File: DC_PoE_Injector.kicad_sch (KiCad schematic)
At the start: 3 parts, among them U1 TPS23861

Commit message: Adding some skeleton
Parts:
- U1: LCSC (none) -> C93245
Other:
- added sheet Connectors (1_Connectors.kicad_sch)
- added sheet Power (2_Power.kicad_sch)

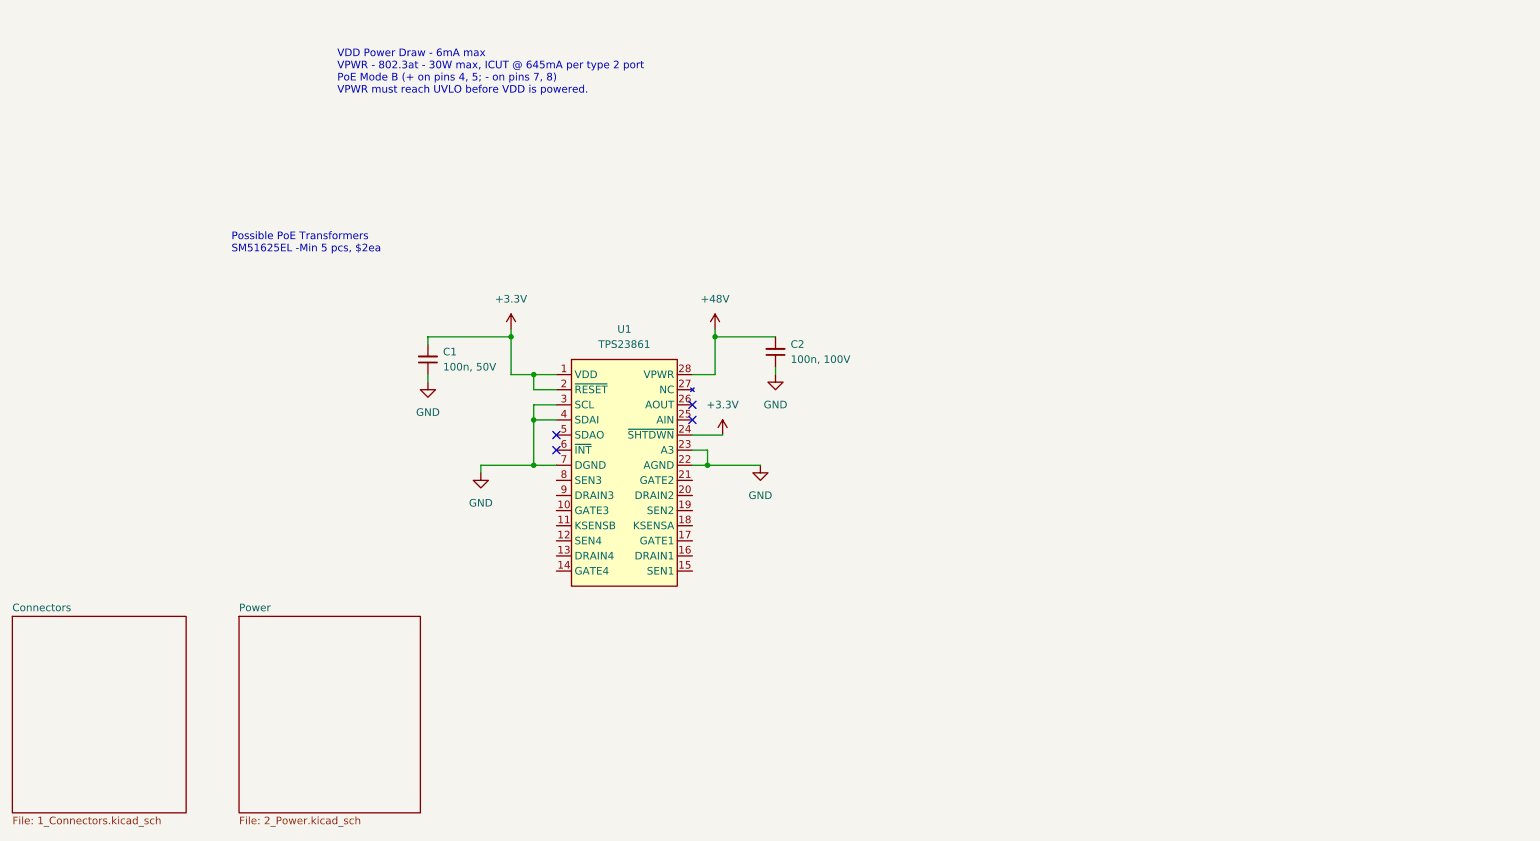
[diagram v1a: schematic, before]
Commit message: Add magnetics for poe
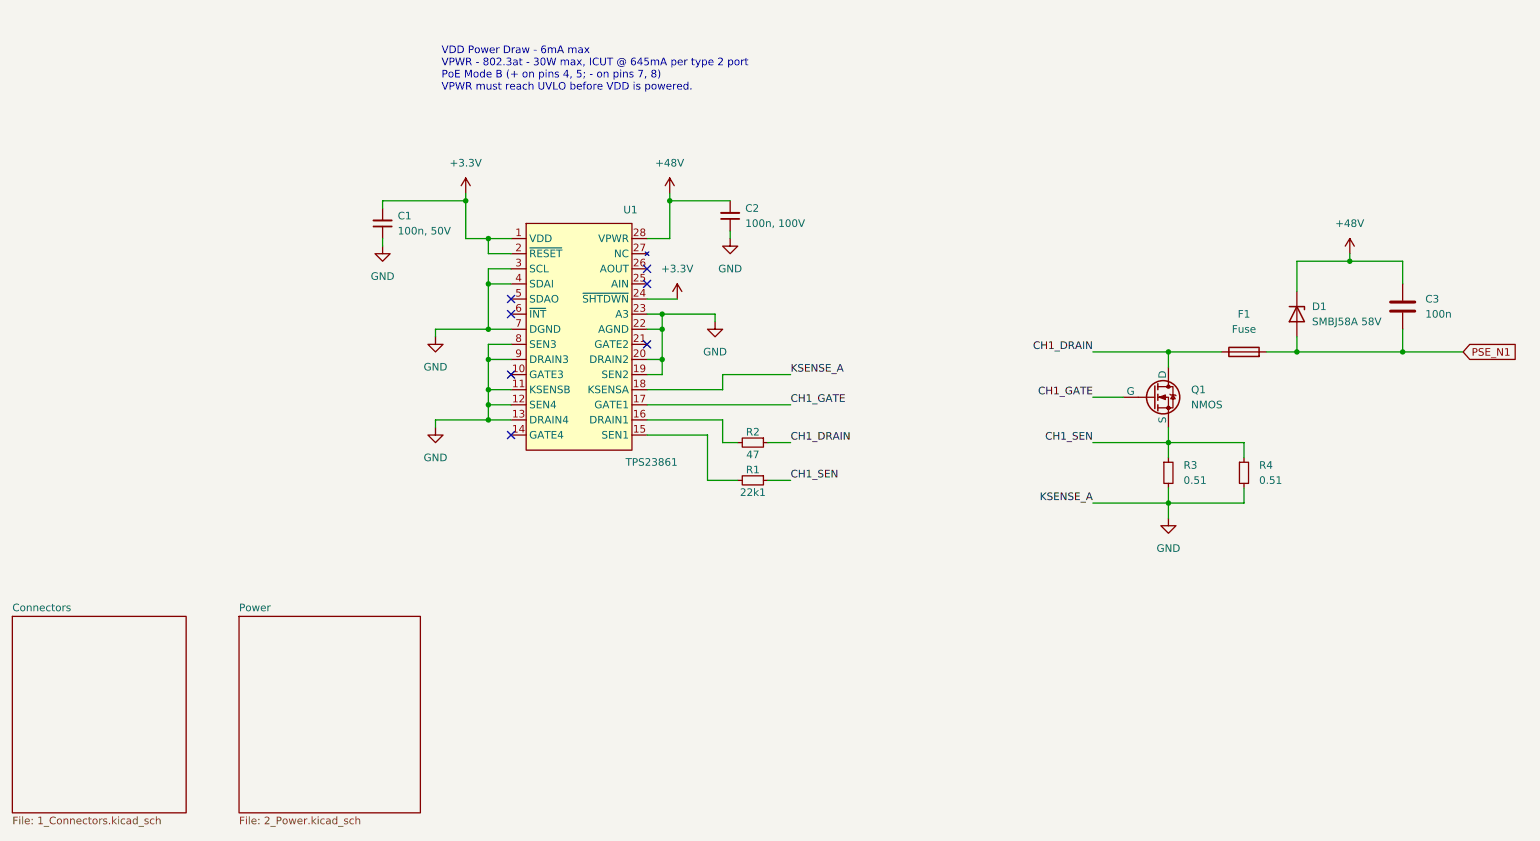
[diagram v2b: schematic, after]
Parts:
- added C3: 100n, symbol Device:C
- added D1: SMBJ58A 58V, symbol Device:D_Zener
- added F1: Fuse, symbol Device:Fuse
- added Q1: NMOS, symbol Simulation_SPICE:NMOS
- added R1: 22k1, symbol Device:R_Small
- added R2: 47, symbol Device:R_Small
- added R3, R4: 0.51, symbol Device:R_Small
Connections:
- net +48V: now also C3.1, D1.1 (K)
- net GND: now also U1.11 (KSENSB), U1.12 (SEN4), U1.13 (DRAIN4), U1.18 (KSENSA), U1.19 (SEN2), U1.20 (DRAIN2), U1.8 (SEN3), U1.9 (DRAIN3), R3.2, R4.2
- net at U1.15 (SEN1): now also R1.2
- net at U1.16 (DRAIN1): now also R2.2
- net CH1_GATE: now reaches U1.17 (GATE1)
- net CH1_GATE: now also Q1.2 (G)
- new net CH1_DRAIN: F1.1, Q1.1 (D), R2.1
- new net CH1_SEN: Q1.3 (S), R1.1, R3.1, R4.1
- new net PSE_N1: C3.2, D1.2 (A), F1.2
- no-connect marks 4 -> 7
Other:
- note removed: "Possible PoE Transformers SM51625EL -Min 5 pcs, $2ea"
- moved on the sheet: C1, C2, U1

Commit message: Add boost converter
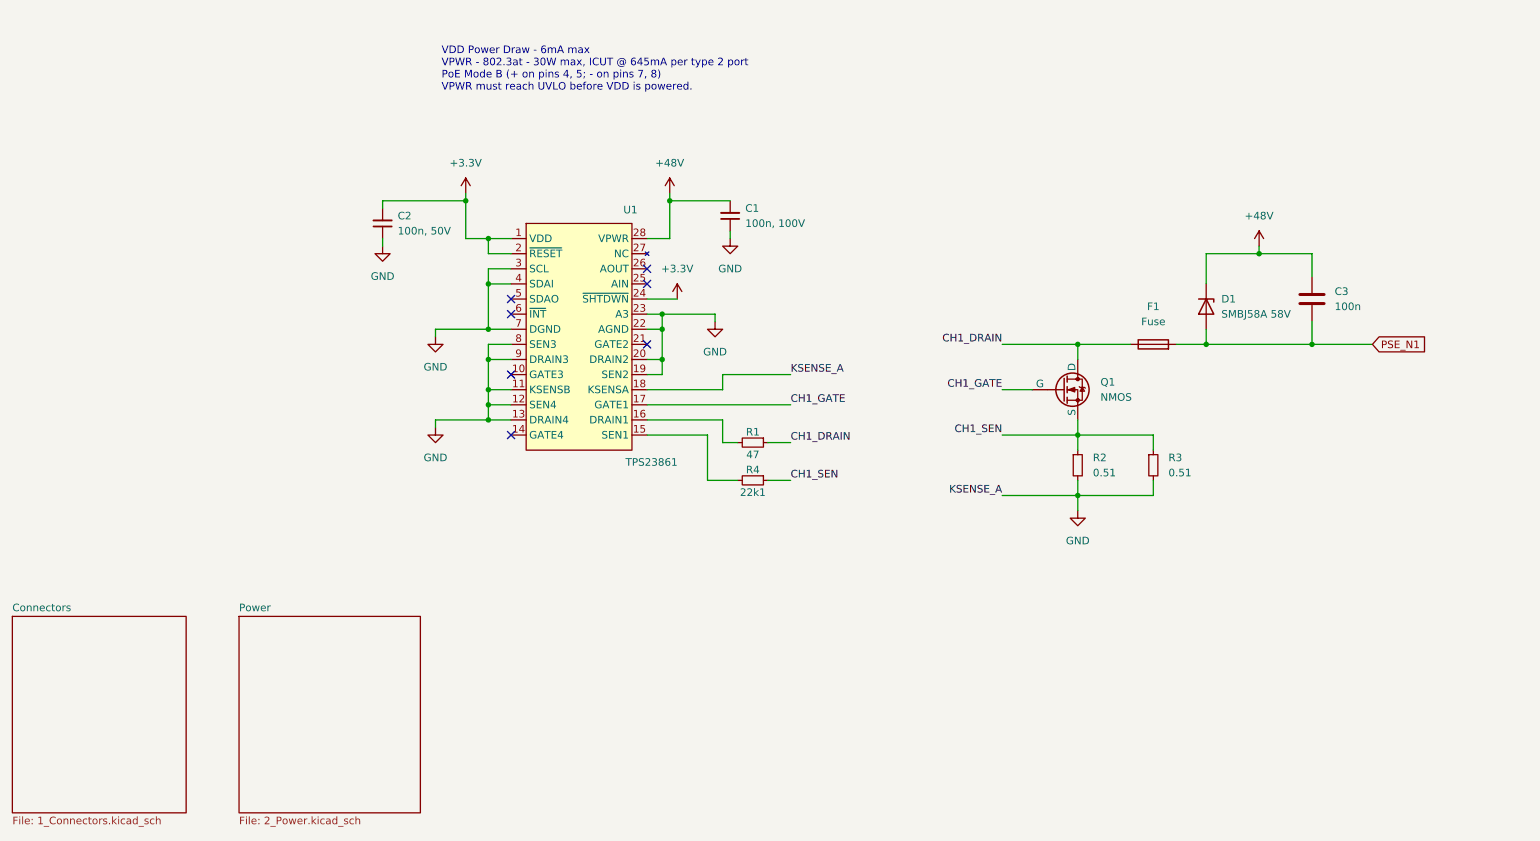
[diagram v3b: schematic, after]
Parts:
- renumbered C2 to C1, C1 to C2, R2 to R1, R3 to R2, R4 to R3, R1 to R4
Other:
- moved on the sheet: C3, D1, F1, Q1, R2, R3

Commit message: finish layout
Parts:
- removed C3: 100n, symbol Device:C
- removed Q1: NMOS, symbol Simulation_SPICE:NMOS
- added C3: 100n, 100V, Capacitor_SMD:C_0805_2012Metric, symbol Device:C_Small
- added C30: 1u, Capacitor_SMD:C_0805_2012Metric, symbol Device:C_Small
- added Q1: IRLR3410TRPBF, Package_TO_SOT_SMD:TO-252-2, symbol Device:Q_NMOS_GDS
- C1: footprint (none) -> Capacitor_SMD:C_0805_2012Metric; LCSC (none) -> C28233
- C2: footprint (none) -> Capacitor_SMD:C_0603_1608Metric; LCSC (none) -> C14663
- D1: footprint (none) -> Diode_SMD:D_SMB; LCSC (none) -> C135085
- F1: value Fuse -> 2920L110/60MR; footprint (none) -> Fuse:Fuse_2920_7451Metric; LCSC (none) -> C315903
- R1: footprint (none) -> Resistor_SMD:R_0603_1608Metric; LCSC (none) -> C23182
- R2, R3: value 0.51 -> 510m 1%; footprint (none) -> Resistor_SMD:R_0805_2012Metric; LCSC (none) -> C491234
- R4: value 22k1 -> 22.1; footprint (none) -> Resistor_SMD:R_0603_1608Metric; LCSC (none) -> C22958
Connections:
- net +3.3V: no longer U1.2 (~{RESET})
- net CH1_DRAIN: now also Q1.2 (D)
- net CH1_GATE: now also Q1.1 (G)
- net CH1_SEN: now also Q1.3 (S)
- net GND: now also C30.1
- net +48V renamed +54V
- net +54V: now also C3.2
- net PSE_N1 renamed POE_78
- net POE_78: now also C3.1
- new net: C30.2, U1.2 (~{RESET})
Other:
- note added: "GATE: 10-12.5V"
- note added: "MOSFET selection criteria: V_DS max >= 100V R_DS(on) between 50-150mOhm C_ISS <= 2000pF Q_G < 50nC"
- note added: "PoE PSE Controller"
- moved on the sheet: C2, D1

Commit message: Some cleanups
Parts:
- Q1: footprint Package_TO_SOT_SMD:TO-252-2 -> CakeKiCadLib:TO-252-2-JLCPCB
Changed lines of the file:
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@@
 			)
 		)
-		(property "Footprint" "Package_TO_SOT_SMD:TO-252-2"
+		(property "Footprint" "CakeKiCadLib:TO-252-2-JLCPCB"
 			(at 203.2 76.2 0)
 			(effects
